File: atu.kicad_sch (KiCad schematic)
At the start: 4 parts, among them U11 74HC157, U12 74HC157, U13 AS7C256C-15PCN, U15 AS7C256C-15PCN

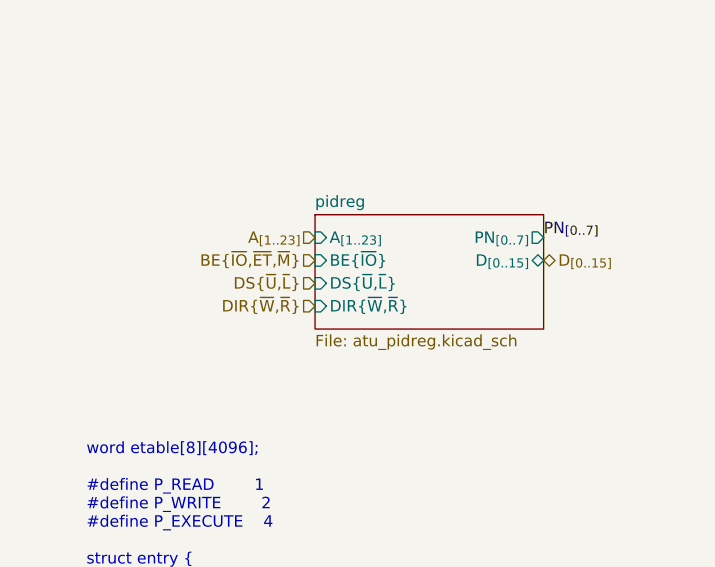
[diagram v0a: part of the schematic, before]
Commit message: finished scheme, footprints not completely assigned yet
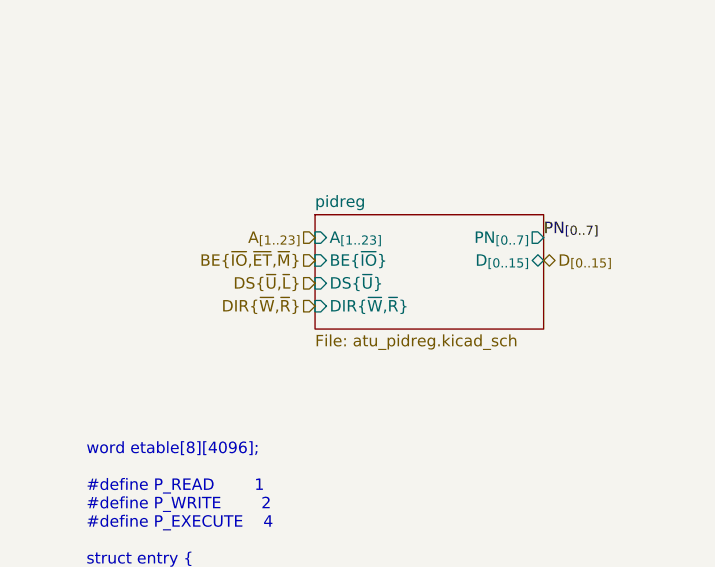
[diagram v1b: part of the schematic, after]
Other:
- sheet pidreg ports: added DS{~{U}}; removed DS{~{U},~{L}}

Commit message: done the pcb layout + added the 1M ram bank project
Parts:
- U11, U12: footprint Package_DIP:DIP-16_W7.62mm_Socket -> Package_DIP:DIP-16_W7.62mm
- U13, U15: footprint (none) -> Package_DIP:DIP-28_W15.24mm
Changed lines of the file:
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@@
 			)
 		)
-		(property "Footprint" ""
+		(property "Footprint" "Package_DIP:DIP-28_W15.24mm"
 			(at 87.63 234.62 0)
 			(effects
@@
 			)
 		)
-		(property "Footprint" ""
+		(property "Footprint" "Package_DIP:DIP-28_W15.24mm"
 			(at 163.83 234.62 0)
 			(effects
@@
 			)
 		)
-		(property "Footprint" "Package_DIP:DIP-16_W7.62mm_Socket"
+		(property "Footprint" "Package_DIP:DIP-16_W7.62mm"
 			(at 63.5 63.5 0)
 			(effects
@@
 			)
 		)
-		(property "Footprint" "Package_DIP:DIP-16_W7.62mm_Socket"
+		(property "Footprint" "Package_DIP:DIP-16_W7.62mm"
 			(at 139.7 63.5 0)
 			(effects

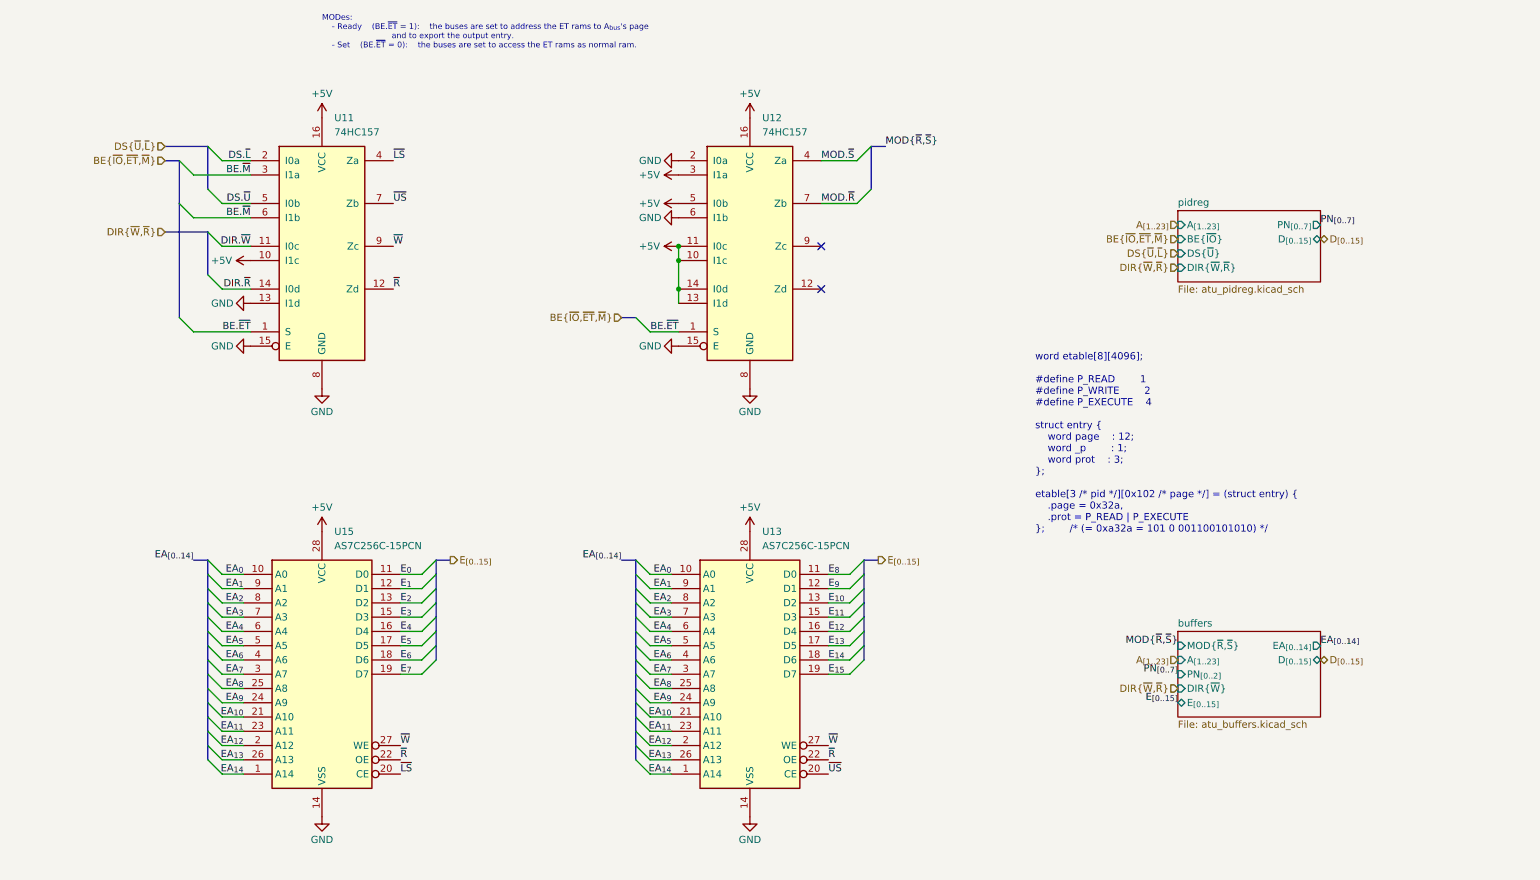
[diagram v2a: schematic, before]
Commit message: first commit: scheme ok [decoder]: 	- new spv. address space [mmu]: 	- removed pidreg 	- switched back to 8Kb mmu rams [ram/peripherals]: 	- added ground pins to connectors [misc]: 	- added DMA support 	- added clock halfer
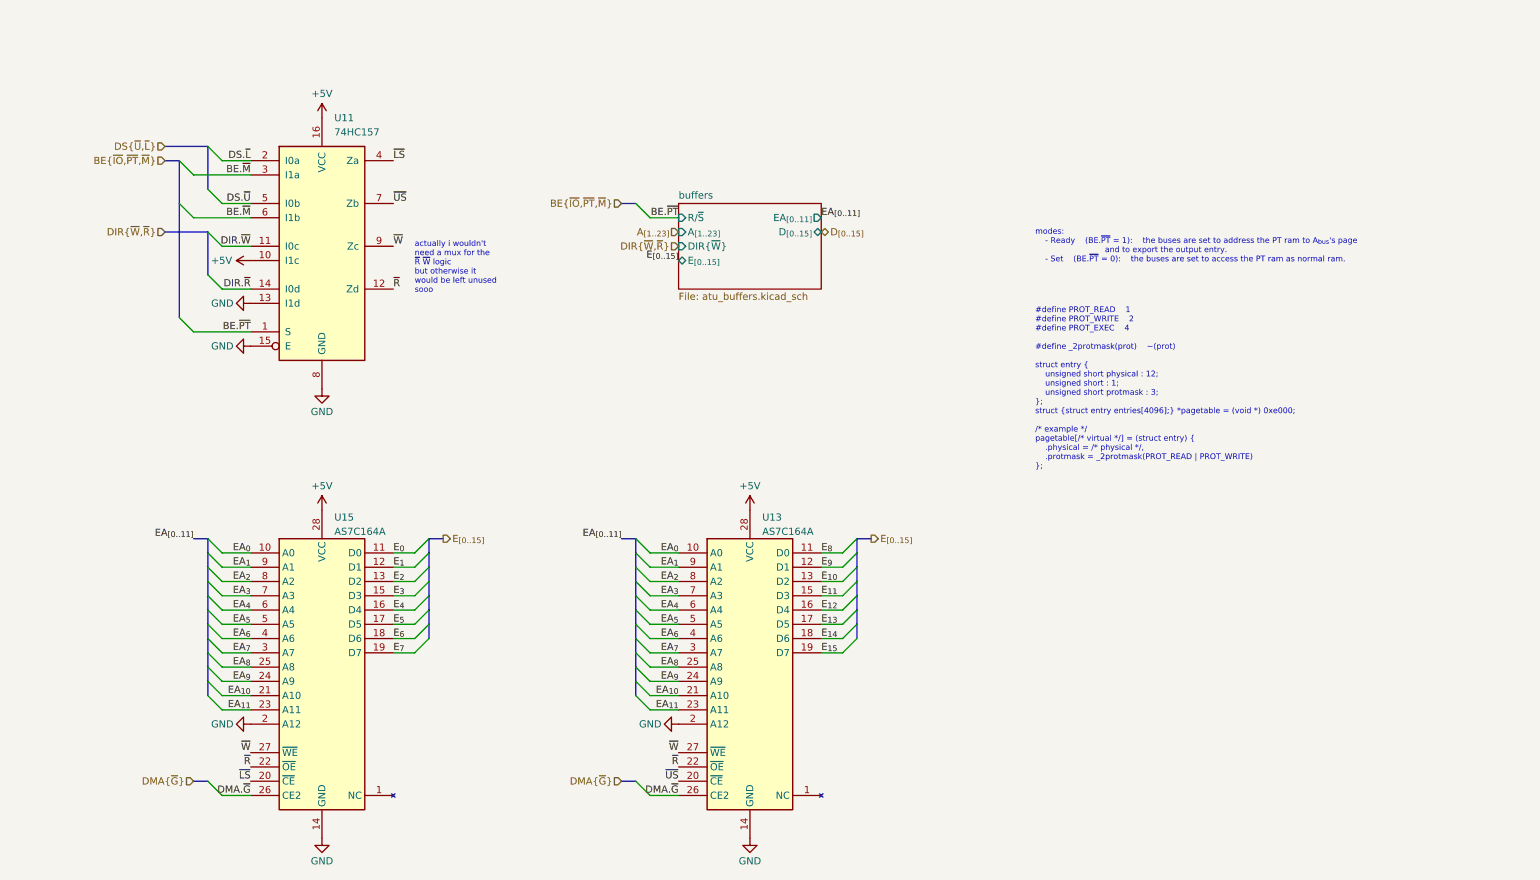
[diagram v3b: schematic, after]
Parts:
- removed U12: 74HC157, Package_DIP:DIP-16_W7.62mm, symbol 74xx:74LS157
- removed U13, U15: AS7C256C-15PCN, Package_DIP:DIP-28_W15.24mm, symbol AS7C256C-15PCN:AS7C256C-15PCN
- added U13, U15: AS7C164A, Package_DIP:DIP-28_W7.62mm_Socket, symbol Memory_RAM:AS7C164A
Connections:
- net +5V: now also U13.28 (VCC), U15.28 (VCC)
- net EA_{0}: now also U13.10 (A0), U15.10 (A0)
- net EA_{10}: now also U13.21 (A10), U15.21 (A10)
- net EA_{11}: now also U13.23 (A11), U15.23 (A11)
- net EA_{1}: now also U13.9 (A1), U15.9 (A1)
- net EA_{2}: now also U13.8 (A2), U15.8 (A2)
- net EA_{3}: now also U13.7 (A3), U15.7 (A3)
- net EA_{4}: now also U13.6 (A4), U15.6 (A4)
- net EA_{5}: now also U13.5 (A5), U15.5 (A5)
- net EA_{6}: now also U13.4 (A6), U15.4 (A6)
- net EA_{7}: now also U13.3 (A7), U15.3 (A7)
- net EA_{8}: now also U13.25 (A8), U15.25 (A8)
- net EA_{9}: now also U13.24 (A9), U15.24 (A9)
- net E_{0}: now also U15.11 (D0)
- net E_{10}: now also U13.13 (D2)
- net E_{11}: now also U13.15 (D3)
- net E_{12}: now also U13.16 (D4)
- net E_{13}: now also U13.17 (D5)
- net E_{14}: now also U13.18 (D6)
- net E_{15}: now also U13.19 (D7)
- net E_{1}: now also U15.12 (D1)
- net E_{2}: now also U15.13 (D2)
- net E_{3}: now also U15.15 (D3)
- net E_{4}: now also U15.16 (D4)
- net E_{5}: now also U15.17 (D5)
- net E_{6}: now also U15.18 (D6)
- net E_{7}: now also U15.19 (D7)
- net E_{8}: now also U13.11 (D0)
- net E_{9}: now also U13.12 (D1)
- net GND: now also U13.14 (GND), U13.2 (A12), U15.14 (GND), U15.2 (A12)
- net ~{LS}: now also U15.20 (~{CE})
- net ~{R}: now also U13.22 (~{OE}), U15.22 (~{OE})
- net ~{US}: now also U13.20 (~{CE})
- net ~{W}: now also U13.27 (~{WE}), U15.27 (~{WE})
- net BE.~{ET} renamed BE.~{PT}
- new net DMA.~{G}: U13.26 (CE2), U15.26 (CE2)
- no-connect marks 2 -> 0
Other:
- removed sheet pidreg
- sheet buffers ports: added EA_{[0..11]}, R/~{S}; removed EA_{[0..14]}, MOD{~{R},~{S}}, PN_{[0..2]}
- note added: "#define PROT_READ 1 #define PROT_WRITE 2 #define PROT_EXEC 4 #define _2protmask(prot) ~(prot) struct entry { unsigned short physical : 12; unsigned short : 1; unsigned short protmask : 3; }; struct {struct entry entries[4096];} *pagetable = (void *) 0xe000; /* example */ pagetable[/* virtual */] = (struct entry) { .physical = /* physical */, .protmask = _2protmask(PROT_READ | PROT_WRITE) };"
- note added: "actually i wouldn't need a mux for the ~{R} ~{W} logic but otherwise it would be left unused sooo"
- note added: "modes: - Ready (BE.~{PT} = 1): the buses are set to address the PT ram to A_{bus}'s page and to export the output entry. - Set (BE.~{PT} = 0): the buses are set to access the PT ram as normal ram."
- note removed: "MODes: - Ready (BE.~{ET} = 1): the buses are set to address the ET rams to A_{bus}'s page and to export the output entry. - Set (BE.~{ET} = 0): the buses are set to access the ET rams as normal ram."
- note removed: "word etable[8][4096]; #define P_READ 1 #define P_WRITE 2 #define P_EXECUTE 4 struct entry { word page : 12; word _p : 1; word prot : 3; }; etable[3 /* pid */][0x102 /* page */] = (struct entry) { .page = 0x32a, .prot = P_READ | P_EXECUTE }; /* (= 0xa32a = 101 0 001100101010) */"
